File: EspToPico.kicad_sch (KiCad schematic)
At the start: 10 parts, among them J1 Conn_01x20_Pin, J2 Conn_01x20_Pin, J3 USB_C_Receptacle_USB2.0_16P, U1 ESP32-S3-WROOM-1, U2 AP2112K-3.3, U3 TPD3E001DRLR

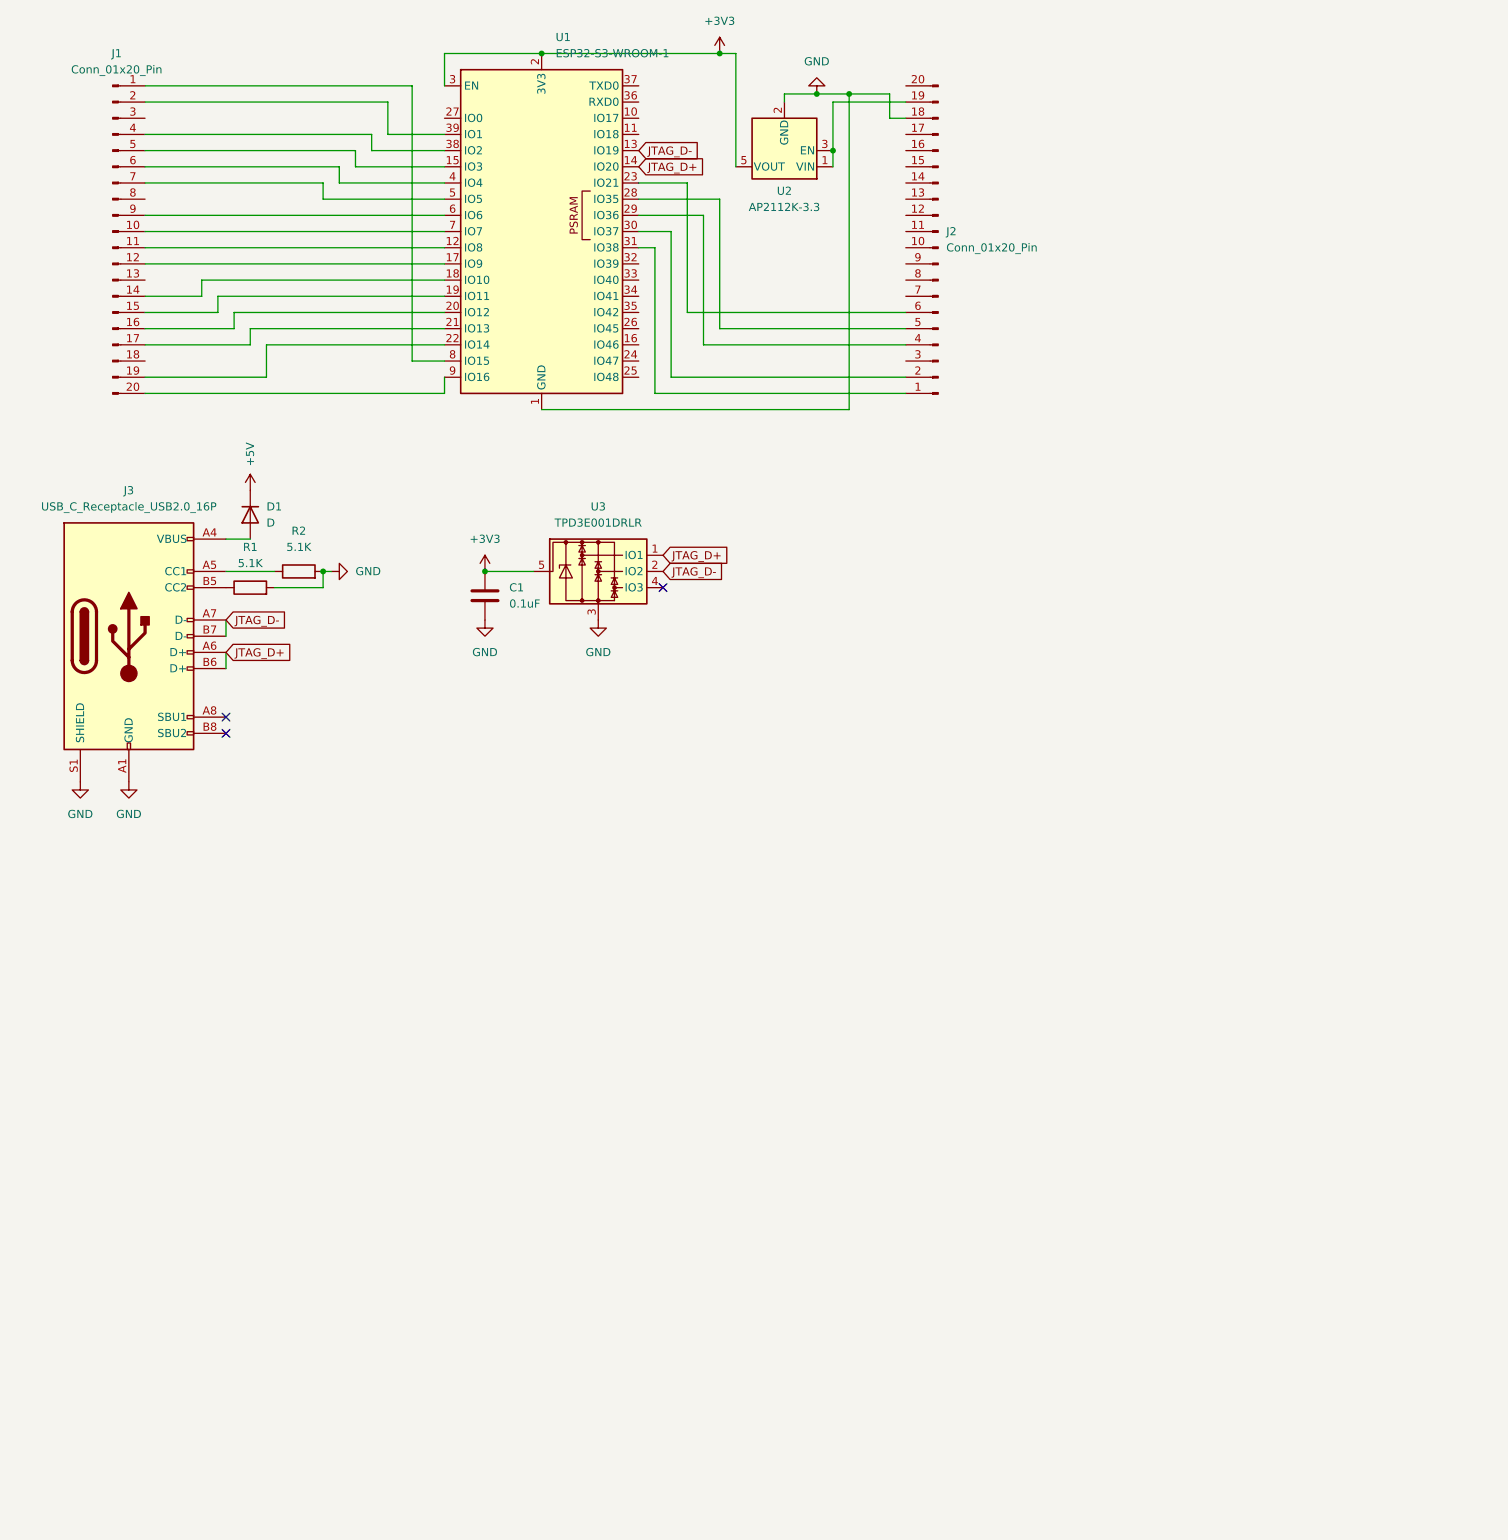
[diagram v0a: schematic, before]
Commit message: Removed sleep depravation
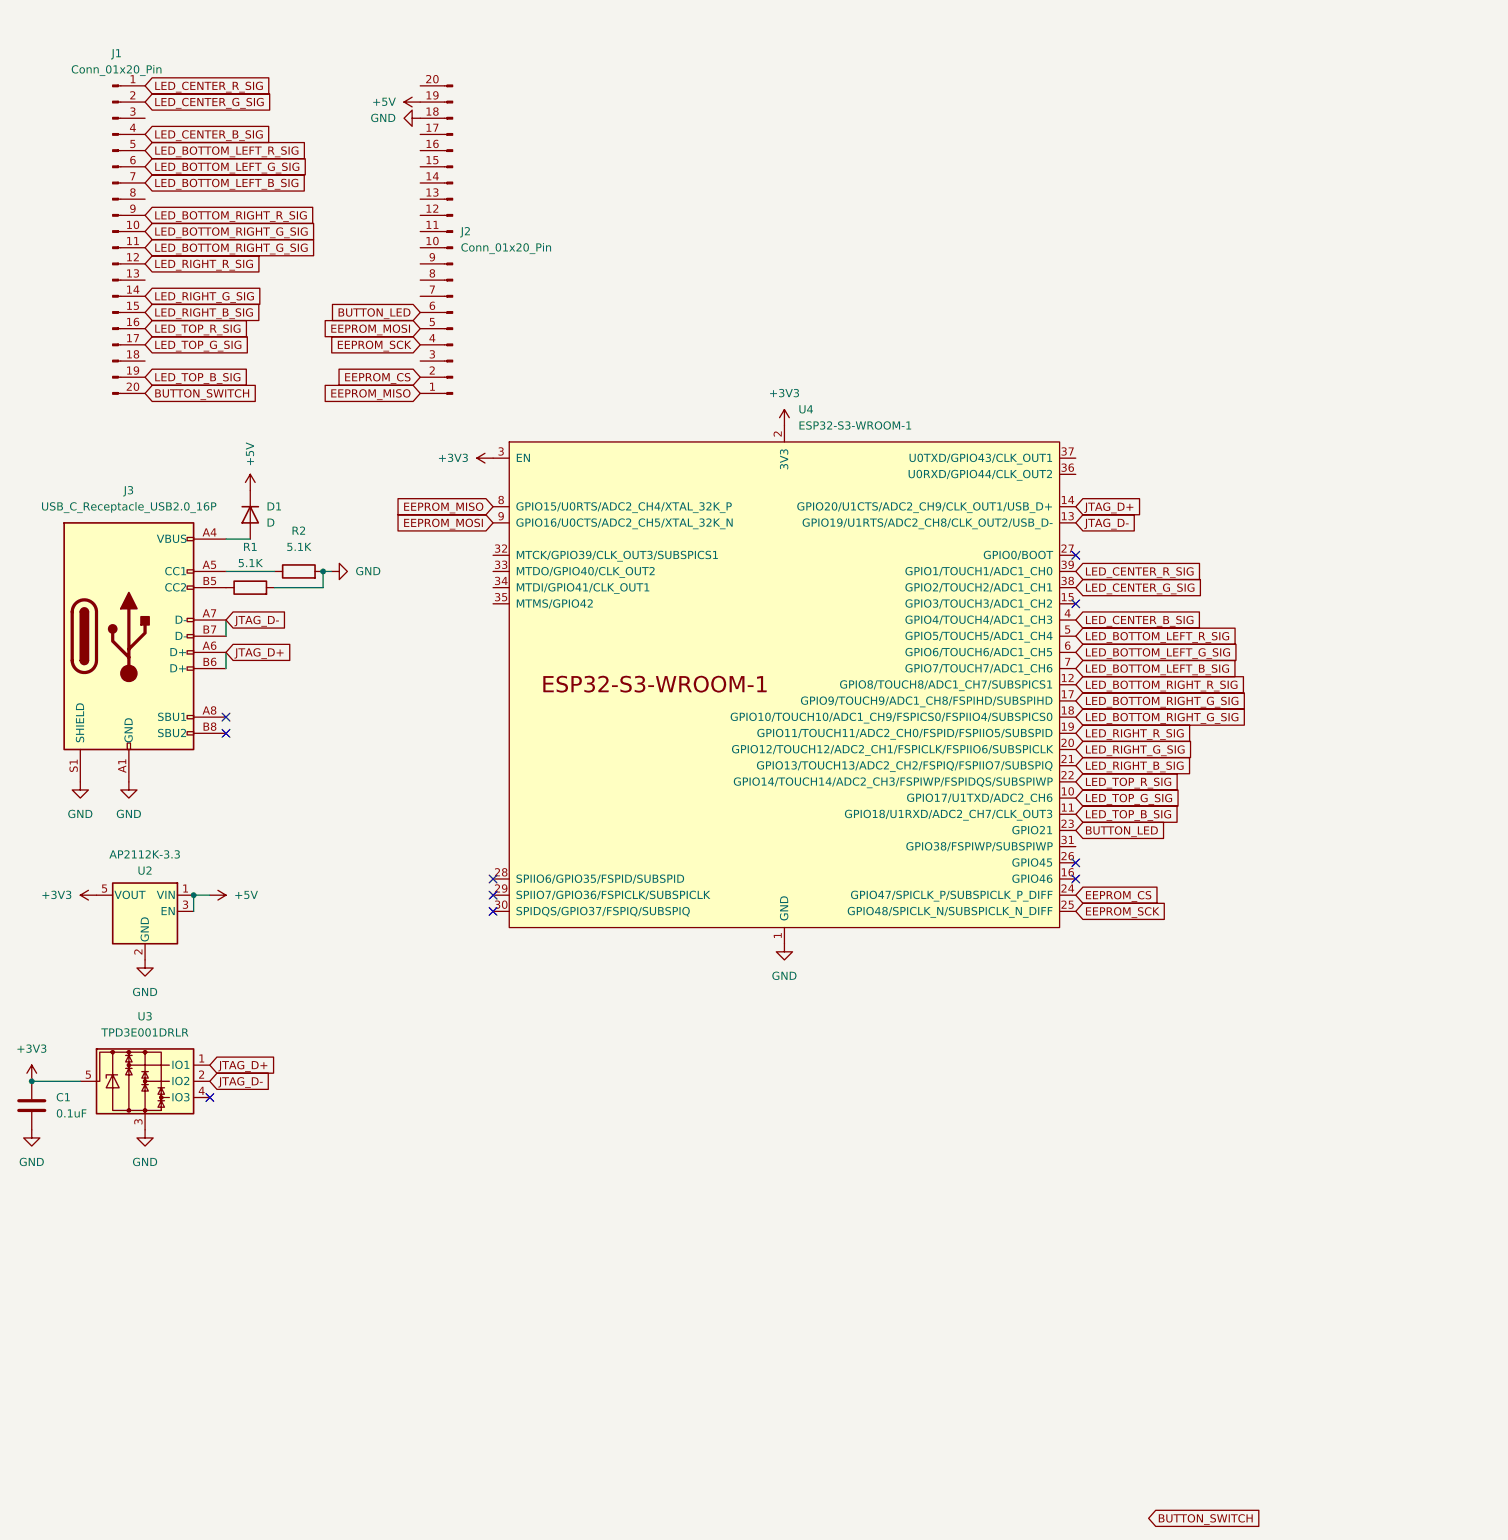
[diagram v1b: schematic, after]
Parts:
- removed U1: ESP32-S3-WROOM-1, RF_Module:ESP32-S3-WROOM-1, symbol RF_Module:ESP32-S3-WROOM-1
- added U4: ESP32-S3-WROOM-1, PCM_Espressif:ESP32-S3-WROOM-1, symbol PCM_Espressif:ESP32-S3-WROOM-1
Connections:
- net +3V3: now also U4.2 (3V3), U4.3 (EN)
- net +5V: now also J2.19 (Pin_19), U2.1 (VIN), U2.3 (EN)
- net GND: now also U4.1 (GND), U4.40 (GND), U4.41 (GND)
- net JTAG_D+: now also U4.14 (GPIO20/U1CTS/ADC2_CH9/CLK_OUT1/USB_D+)
- net JTAG_D-: now also U4.13 (GPIO19/U1RTS/ADC2_CH8/CLK_OUT2/USB_D-)
- net EEPROM_MISO: now reaches J2.1 (Pin_1)
- net EEPROM_MISO: now also U4.8 (GPIO15/U0RTS/ADC2_CH4/XTAL_32K_P)
- net EEPROM_CS: now reaches J2.2 (Pin_2)
- net EEPROM_CS: now also U4.24 (GPIO47/SPICLK_P/SUBSPICLK_P_DIFF)
- net EEPROM_SCK: now reaches J2.4 (Pin_4)
- net EEPROM_SCK: now also U4.25 (GPIO48/SPICLK_N/SUBSPICLK_N_DIFF)
- net EEPROM_MOSI: now reaches J2.5 (Pin_5)
- net EEPROM_MOSI: now also U4.9 (GPIO16/U0CTS/ADC2_CH5/XTAL_32K_N)
- net BUTTON_LED: now reaches J2.6 (Pin_6)
- net BUTTON_LED: now also U4.23 (GPIO21)
- net LED_CENTER_R_SIG: now reaches J1.1 (Pin_1)
- net LED_CENTER_R_SIG: now also U4.39 (GPIO1/TOUCH1/ADC1_CH0)
- net LED_BOTTOM_RIGHT_G_SIG: now reaches J1.10 (Pin_10)
- net LED_BOTTOM_RIGHT_G_SIG: now also J1.11 (Pin_11), U4.17 (GPIO9/TOUCH9/ADC1_CH8/FSPIHD/SUBSPIHD), U4.18 (GPIO10/TOUCH10/ADC1_CH9/FSPICS0/FSPIIO4/SUBSPICS0)
- net LED_RIGHT_R_SIG: now reaches J1.12 (Pin_12)
- net LED_RIGHT_R_SIG: now also U4.19 (GPIO11/TOUCH11/ADC2_CH0/FSPID/FSPIIO5/SUBSPID)
- net LED_RIGHT_G_SIG: now reaches J1.14 (Pin_14)
- net LED_RIGHT_G_SIG: now also U4.20 (GPIO12/TOUCH12/ADC2_CH1/FSPICLK/FSPIIO6/SUBSPICLK)
- net LED_RIGHT_B_SIG: now reaches J1.15 (Pin_15)
- net LED_RIGHT_B_SIG: now also U4.21 (GPIO13/TOUCH13/ADC2_CH2/FSPIQ/FSPIIO7/SUBSPIQ)
- net LED_TOP_R_SIG: now reaches J1.16 (Pin_16)
- net LED_TOP_R_SIG: now also U4.22 (GPIO14/TOUCH14/ADC2_CH3/FSPIWP/FSPIDQS/SUBSPIWP)
- net LED_TOP_G_SIG: now reaches J1.17 (Pin_17)
- net LED_TOP_G_SIG: now also U4.10 (GPIO17/U1TXD/ADC2_CH6)
- net LED_TOP_B_SIG: now reaches J1.19 (Pin_19)
- net LED_TOP_B_SIG: now also U4.11 (GPIO18/U1RXD/ADC2_CH7/CLK_OUT3)
- net LED_CENTER_G_SIG: now reaches J1.2 (Pin_2)
- net LED_CENTER_G_SIG: now also U4.38 (GPIO2/TOUCH2/ADC1_CH1)
- net BUTTON_SWITCH: now reaches J1.20 (Pin_20)
- net LED_CENTER_B_SIG: now reaches J1.4 (Pin_4)
- net LED_CENTER_B_SIG: now also U4.4 (GPIO4/TOUCH4/ADC1_CH3)
- net LED_BOTTOM_LEFT_R_SIG: now reaches J1.5 (Pin_5)
- net LED_BOTTOM_LEFT_R_SIG: now also U4.5 (GPIO5/TOUCH5/ADC1_CH4)
- net LED_BOTTOM_LEFT_G_SIG: now reaches J1.6 (Pin_6)
- net LED_BOTTOM_LEFT_G_SIG: now also U4.6 (GPIO6/TOUCH6/ADC1_CH5)
- net LED_BOTTOM_LEFT_B_SIG: now reaches J1.7 (Pin_7)
- net LED_BOTTOM_LEFT_B_SIG: now also U4.7 (GPIO7/TOUCH7/ADC1_CH6)
- net LED_BOTTOM_RIGHT_R_SIG: now reaches J1.9 (Pin_9)
- net LED_BOTTOM_RIGHT_R_SIG: now also U4.12 (GPIO8/TOUCH8/ADC1_CH7/SUBSPICS1)
- no-connect marks 3 -> 10
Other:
- moved on the sheet: C1, J2, U3

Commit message: Layout
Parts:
- added C2: 0.1uF, Capacitor_SMD:C_0402_1005Metric, symbol Device:C
- J1, J2: footprint (none) -> Connector_PinHeader_2.54mm:PinHeader_1x20_P2.54mm_Vertical
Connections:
- net +3V3: now also C2.1
- net BUTTON_SWITCH: now also U4.31 (GPIO38/FSPIWP/SUBSPIWP)
- net GND: now also J1.13 (Pin_13), J1.18 (Pin_18), J1.3 (Pin_3), J1.8 (Pin_8), J2.13 (Pin_13), J2.3 (Pin_3), J2.8 (Pin_8), C2.2
- net LED_BOTTOM_RIGHT_G_SIG: no longer J1.11 (Pin_11), U4.18 (GPIO10/TOUCH10/ADC1_CH9/FSPICS0/FSPIIO4/SUBSPICS0)
- new net LED_BOTTOM_RIGHT_B_SIG: J1.11 (Pin_11), U4.18 (GPIO10/TOUCH10/ADC1_CH9/FSPICS0/FSPIIO4/SUBSPICS0)
- no-connect marks 10 -> 26

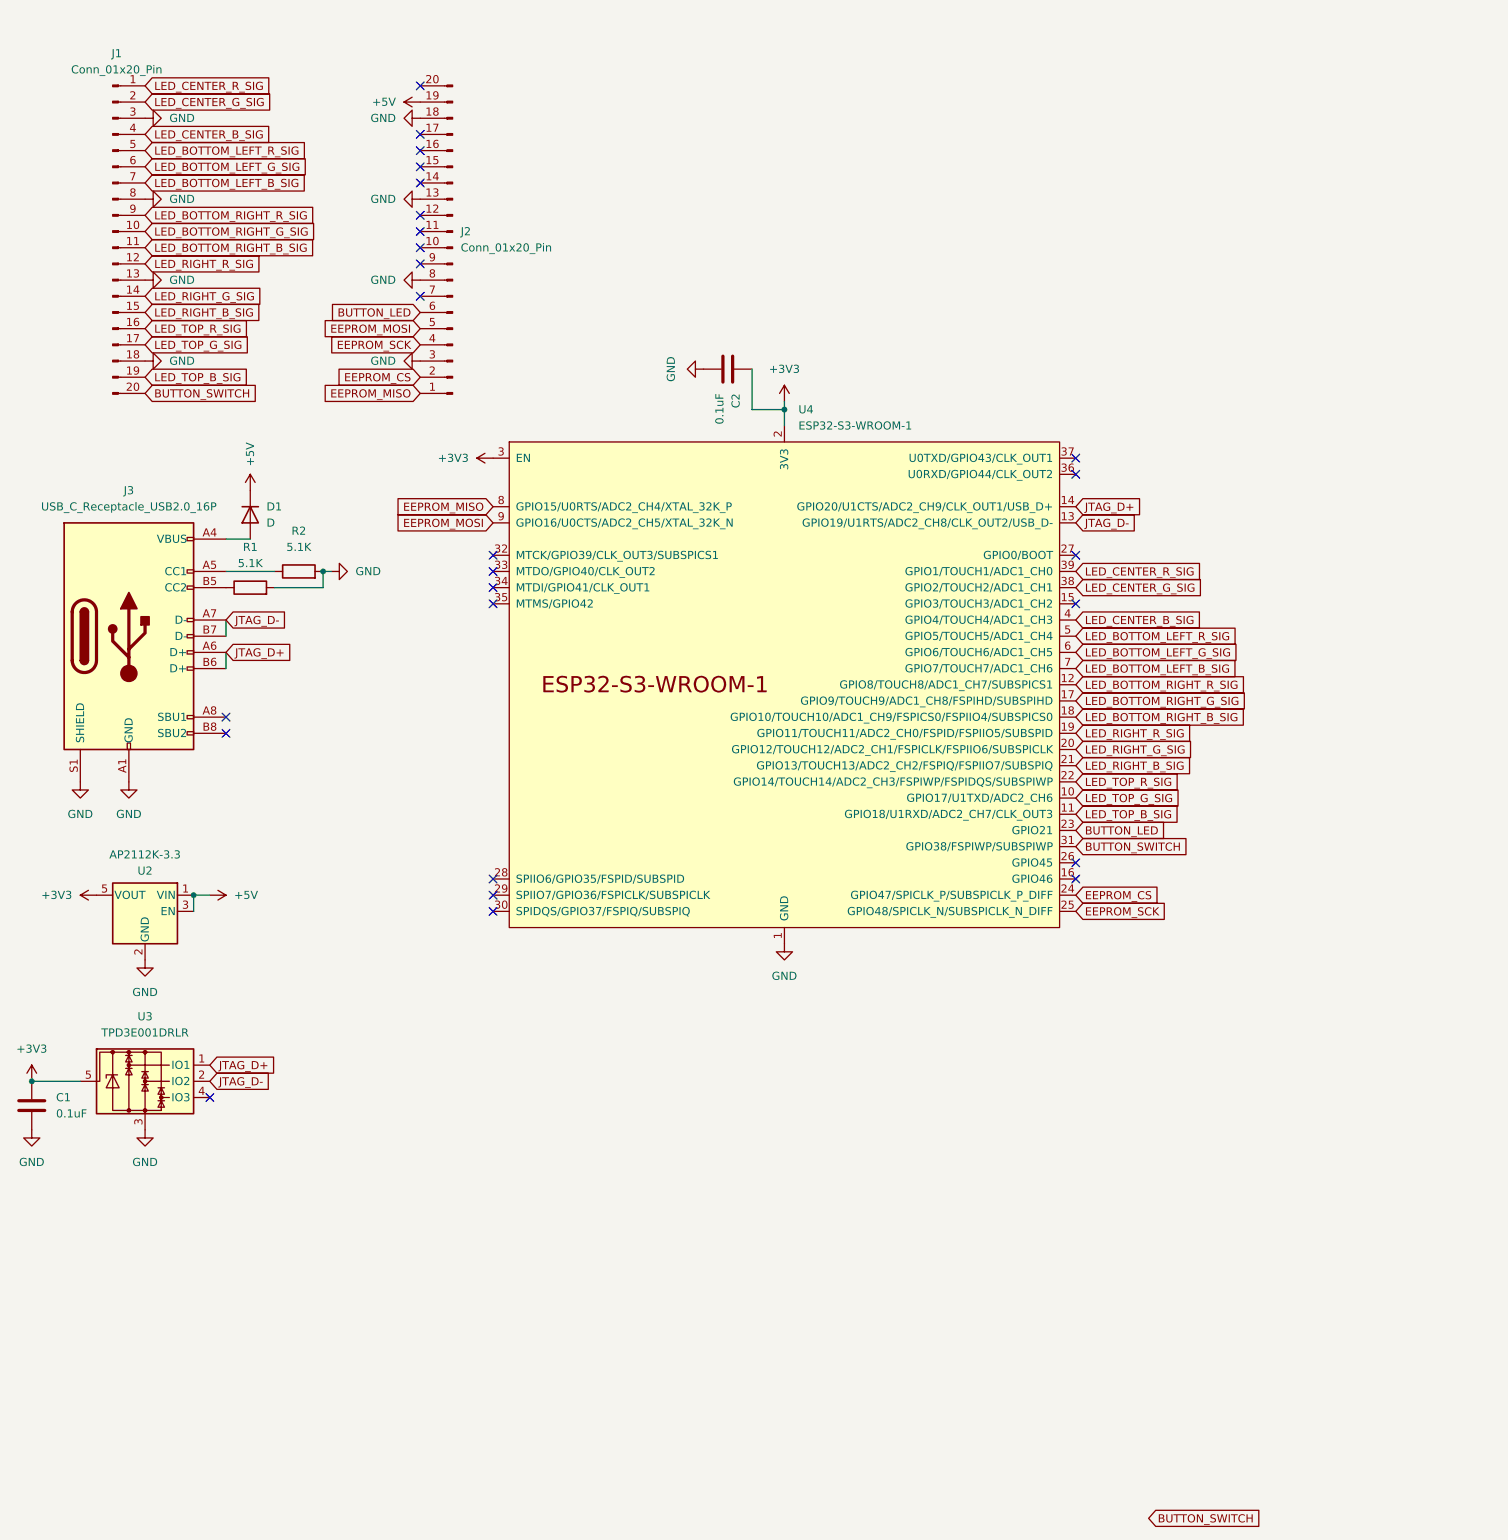
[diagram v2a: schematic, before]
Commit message: Added capacitors to the voltage regulator, added through-hole to the ESP32 for hand-soldering, and updated some routing.
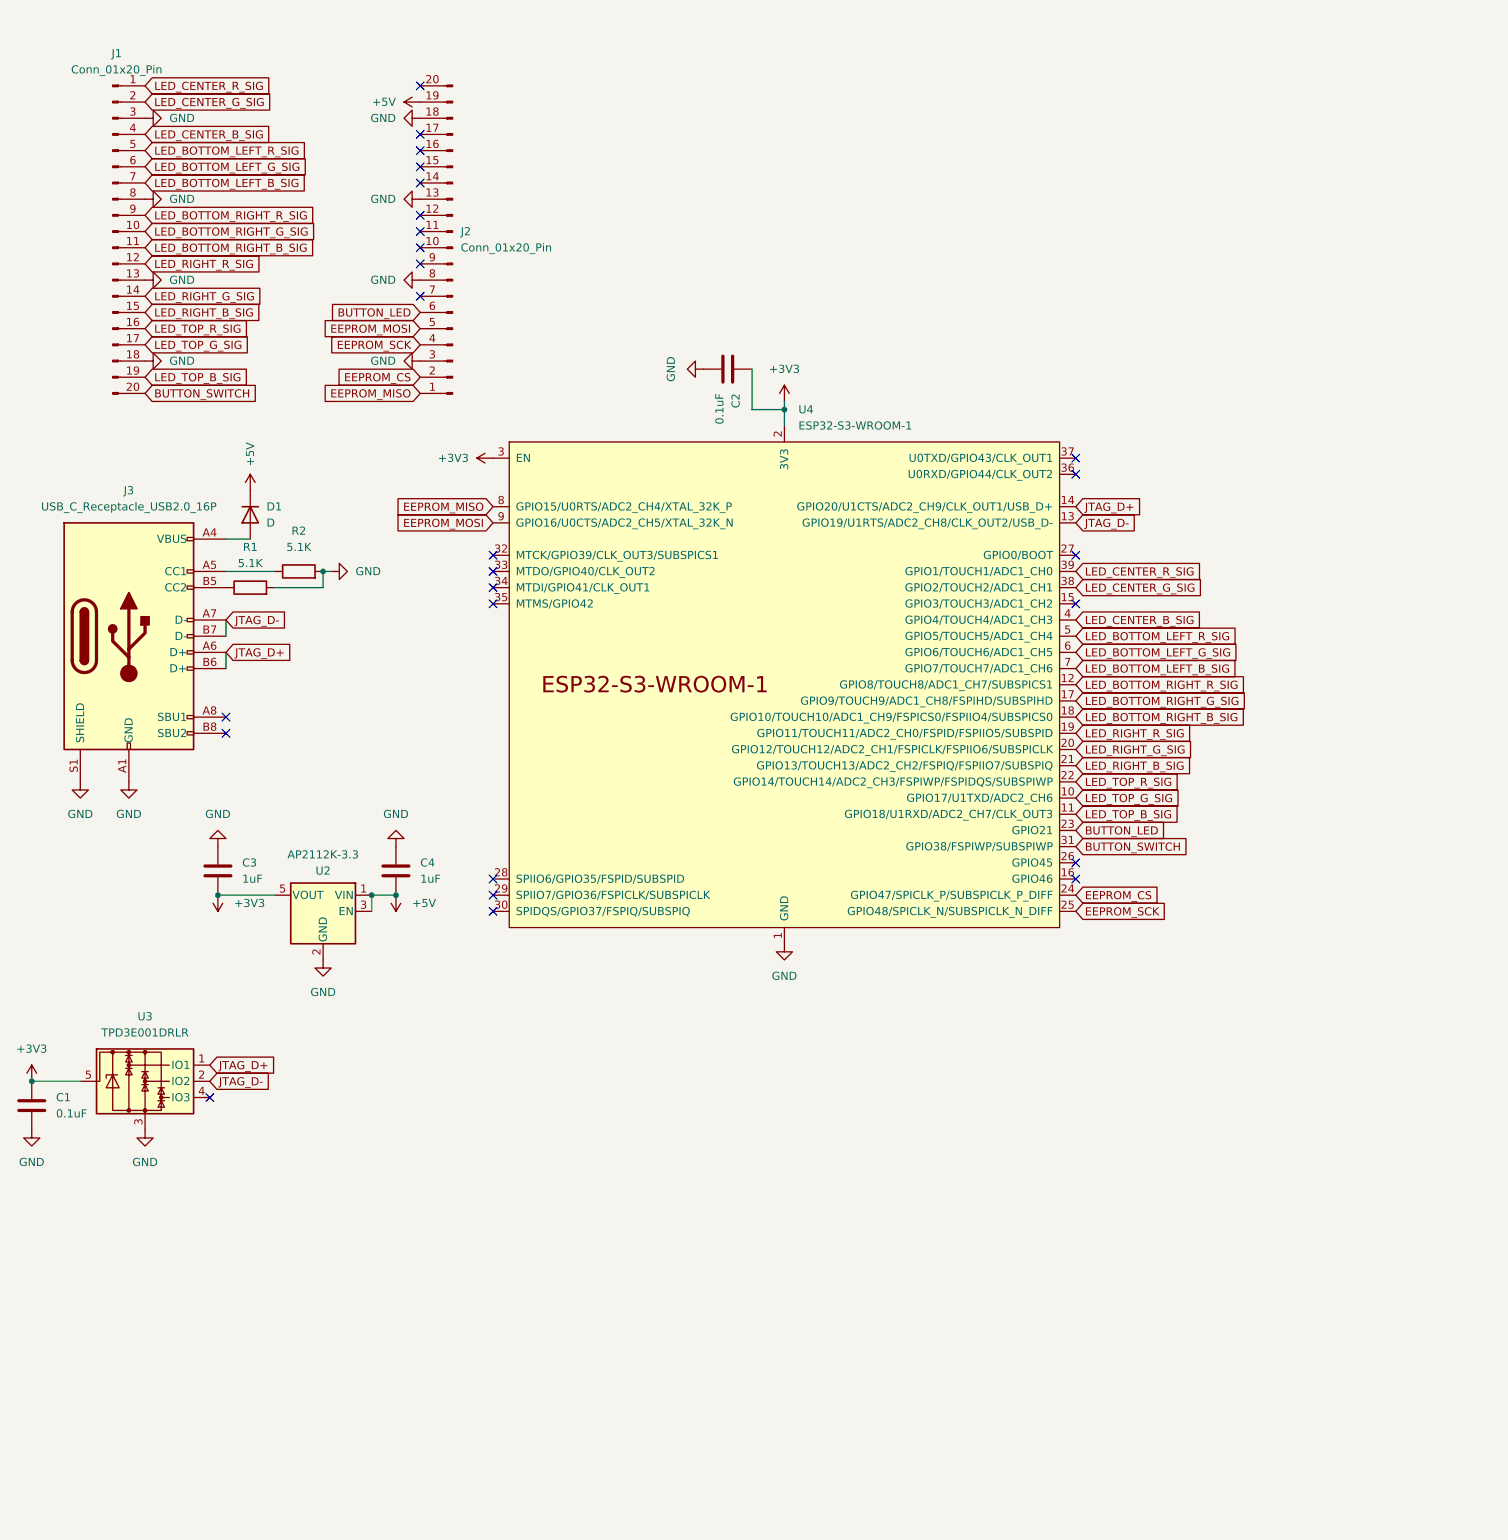
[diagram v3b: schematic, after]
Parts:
- added C3, C4: 1uF, Capacitor_SMD:C_0402_1005Metric, symbol Device:C
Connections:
- net +3V3: now also C3.2
- net +5V: now also C4.2
- net GND: now also C3.1, C4.1
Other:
- moved on the sheet: U2
